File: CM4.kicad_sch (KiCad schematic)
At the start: 5 parts, among them J1 Conn_02x05_Odd_Even, J2 HDMI_A_2.0, U1 RaspberryPi-CM4Lite

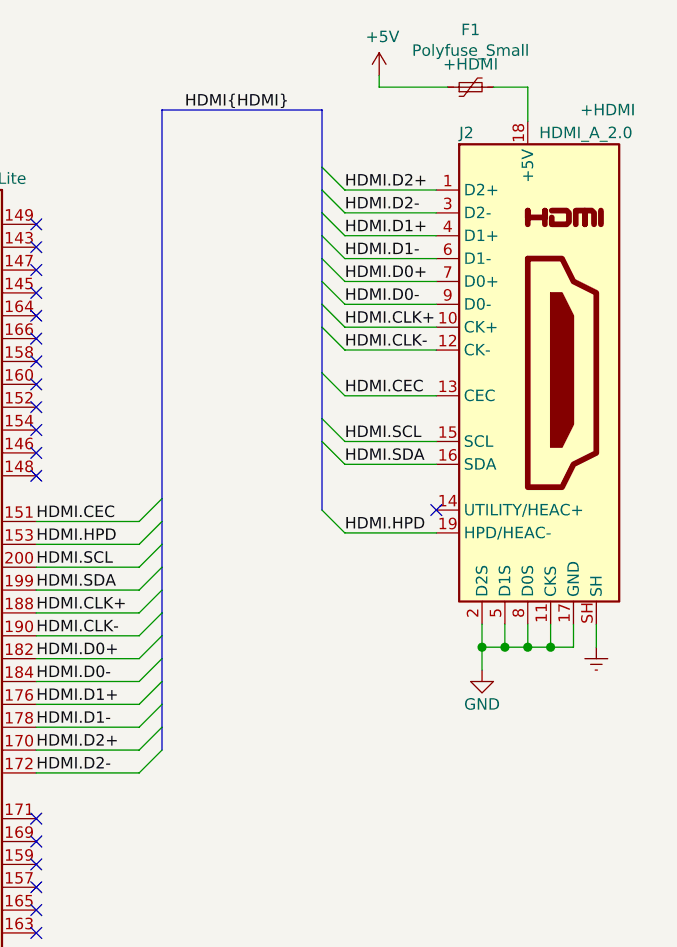
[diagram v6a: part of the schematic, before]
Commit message: Standardize page settings/add page titles
Signed-off-by: Stefan Agner <stefan@agner.ch>
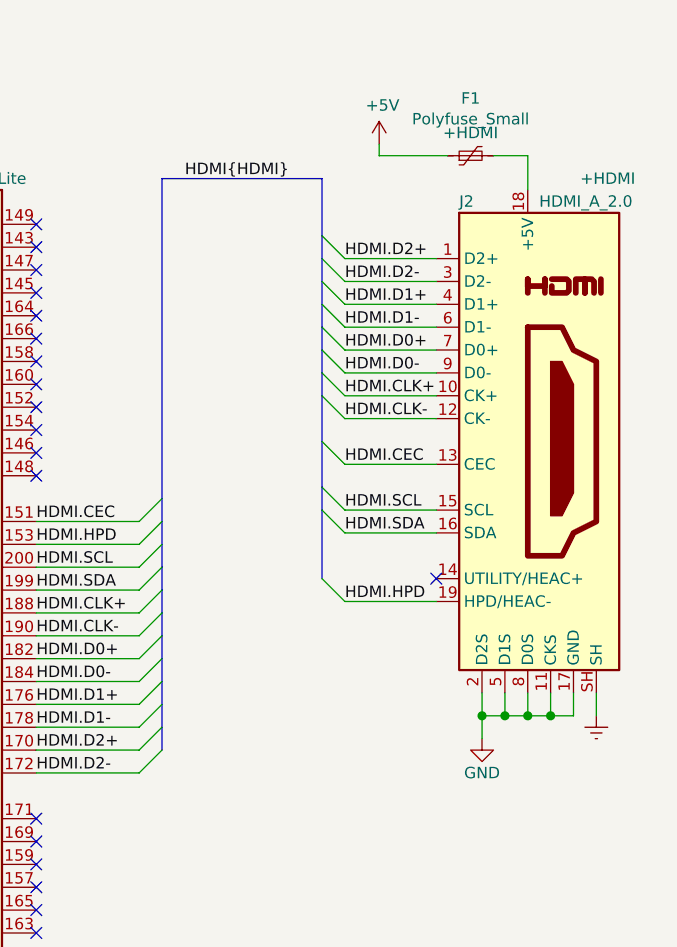
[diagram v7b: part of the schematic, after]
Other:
- company: (none) -> Nabu Casa
- title: (none) -> Compute Module 4
- moved on the sheet: F1, J2

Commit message: Define more footprints and update Manufacturer/PartNumber fields
Signed-off-by: Stefan Agner <stefan@agner.ch>
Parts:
- U1: Manufacturer (none) -> Raspberry Pi Foundation; PartNumber (none) -> CM4002016
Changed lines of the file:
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@@
     (comment 2 "Light Blue")
   )
+  (bus_alias "PCIe" (members "~RST" "~CLKREQ" "CLK+" "CLK-" "TX+" "TX-" "RX+" "RX-"))
+  (bus_alias "SD" (members "D[0..3]" "CMD" "CLK" "PWR" "DET"))
+  (bus_alias "HDMI" (members "D0+" "D0-" "D1+" "D1-" "D2+" "D2-" "CLK+" "CLK-" "CEC" "HPD" "SDA" "SCL"))
   (bus_alias "UART" (members "TXD" "RXD" "CTS" "RTS"))
-  (bus_alias "HDMI" (members "D0+" "D0-" "D1+" "D1-" "D2+" "D2-" "CLK+" "CLK-" "CEC" "HPD" "SDA" "SCL"))
-  (bus_alias "SD" (members "D[0..3]" "CMD" "CLK" "PWR" "DET"))
-  (bus_alias "PCIe" (members "~RST" "~CLKREQ" "CLK+" "CLK-" "TX+" "TX-" "RX+" "RX-"))
   (junction (at 130.81 166.37) (diameter 0.9144) (color 0 0 0 0))
   (junction (at 260.35 90.17) (diameter 1.016) (color 0 0 0 0))
@@
       (effects (font (size 1.27 1.27)) hide)
     )
+    (property "Manufacturer" "Raspberry Pi Foundation" (id 4) (at 185.42 88.9 0)
+      (effects (font (size 1.27 1.27)) hide)
+    )
+    (property "PartNumber" "CM4002016" (id 5) (at 185.42 88.9 0)
+      (effects (font (size 1.27 1.27)) hide)
+    )
   )
   (symbol (lib_id "LightBlue:RaspberryPi-CM4Lite") (at 63.5 88.9 0) (unit 1)
@@
       (effects (font (size 1.27 1.27)) hide)
     )
+    (property "Manufacturer" "Raspberry Pi Foundation" (id 4) (at 63.5 88.9 0)
+      (effects (font (size 1.27 1.27)) hide)
+    )
+    (property "PartNumber" "CM4002016" (id 5) (at 63.5 88.9 0)
+      (effects (font (size 1.27 1.27)) hide)
+    )
